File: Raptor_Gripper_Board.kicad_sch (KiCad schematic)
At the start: 14 parts

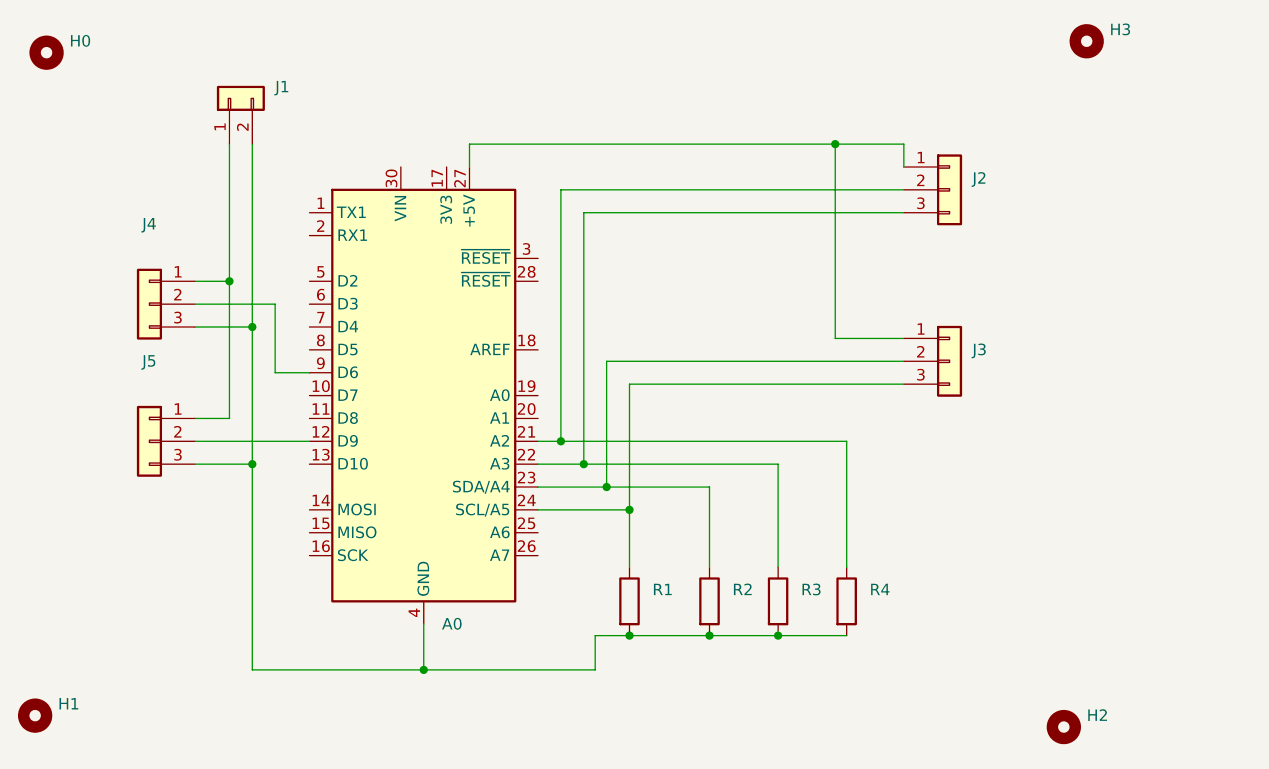
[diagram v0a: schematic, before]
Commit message: added support for third servo
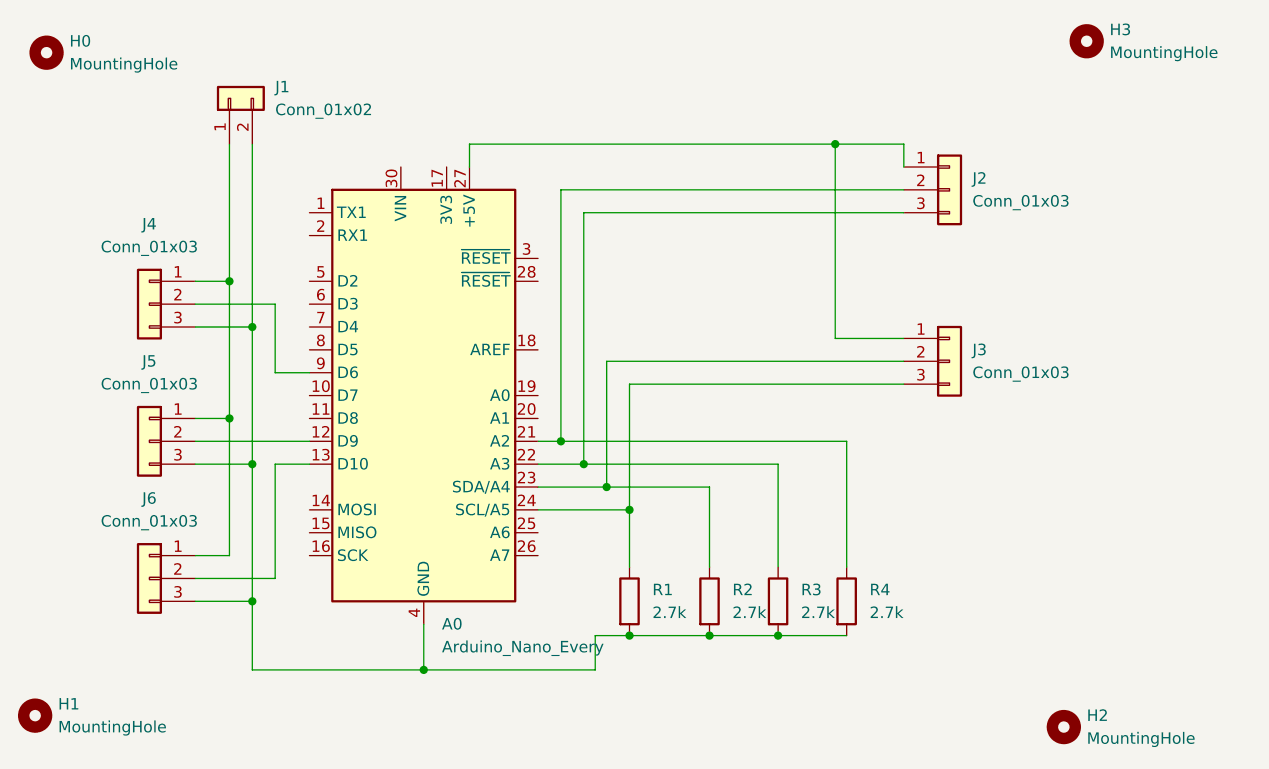
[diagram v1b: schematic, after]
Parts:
- added J6: Conn_01x03, Connector_JST:JST_XH_B3B-XH-A_1x03_P2.50mm_Vertical, symbol Connector_Generic:Conn_01x03
- A0: value (none) -> Arduino_Nano_Every; footprint (none) -> Module:Arduino_Nano
- H0, H1, H2, H3: value (none) -> MountingHole; footprint (none) -> MountingHole:MountingHole_2.2mm_M2_DIN965_Pad_TopBottom
- J1: value (none) -> Conn_01x02; footprint (none) -> Connector_JST:JST_XH_B2B-XH-A_1x02_P2.50mm_Vertical
- J2, J3, J4, J5: value (none) -> Conn_01x03; footprint (none) -> Connector_JST:JST_XH_B3B-XH-A_1x03_P2.50mm_Vertical
- R1, R2, R3, R4: value (none) -> 2.7k; footprint (none) -> Resistor_SMD:R_0805_2012Metric_Pad1.20x1.40mm_HandSolder
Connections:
- net at A0.29 (GND), A0.4 (GND), J1.2 (Pin_2)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: now also J6.3 (Pin_3)
- net at J1.1 (Pin_1), J4.1 (Pin_1), J5.1 (Pin_1): now also J6.1 (Pin_1)
- net at A0.13 (D10): now also J6.2 (Pin_2)
